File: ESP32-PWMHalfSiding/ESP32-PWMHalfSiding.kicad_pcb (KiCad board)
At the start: 2 copper layers, 115.6 x 130.8 mm, 60 parts, among them IC1 MCT6H, IC2 MCT6H, J1 RJ45, J2 RJ45, P601 C A0 A1 A2 A3 A4 A5 A6 A7, P602 C B0 B1 B2 B3 B4 B5 B6 B7, T1 + 15 in -, T2 + 15 out -, T3 In Track1 Out, T4 Motor 1, T5 Motor 2, T6 In Track1 Out, T601 + 12V -, U0 ESP32_DEVKIT_C or TTGO-T1, U0A TTGO-T1, U1 TCAN332DR, U2 SN65HVD233-HT, U3 LM2574N-5.0, U601 PCA9685, U602 TBD62X83A, U603 TBD62X83A, U7 TC4428, U8 TC4428, U9 74HCT00

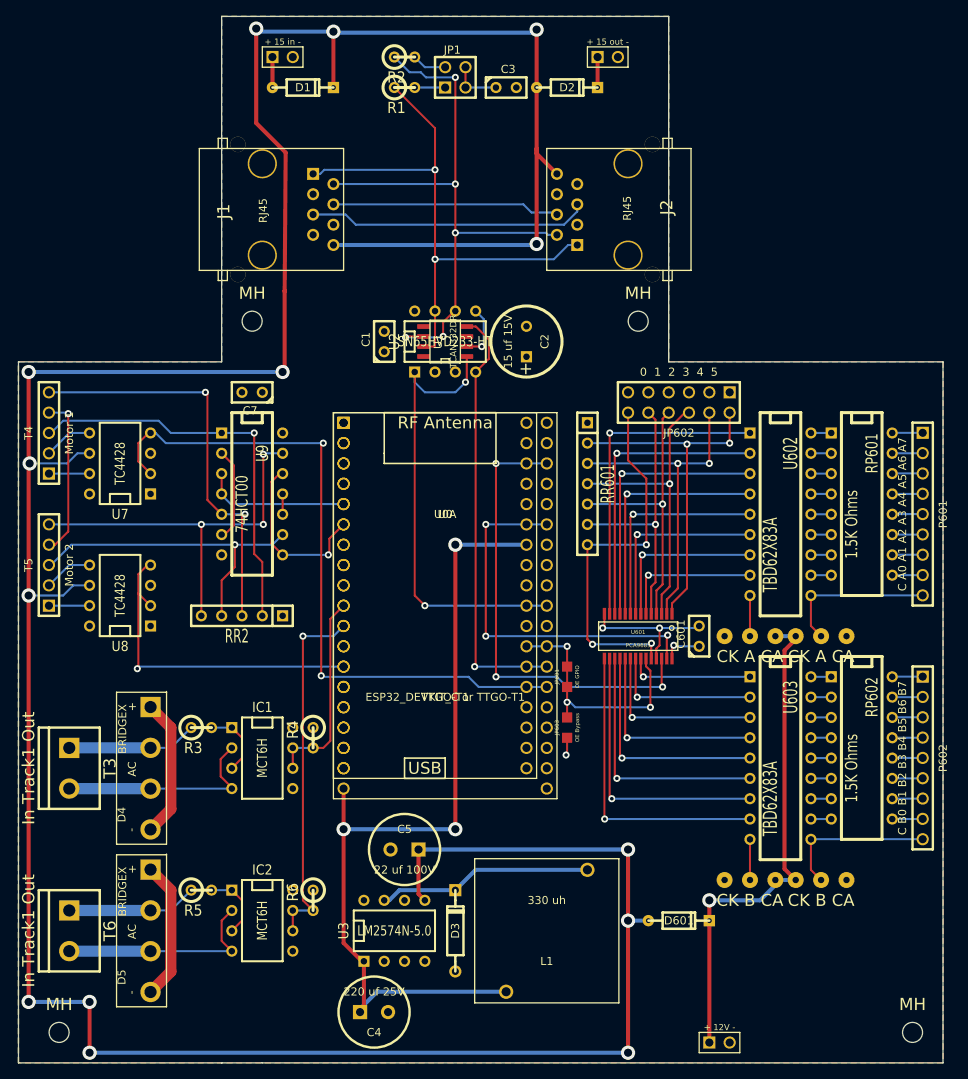
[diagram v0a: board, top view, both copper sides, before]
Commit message: Remove unneeded address jumpers from ESP32-PWMHalfSiding and fixup board part labels.
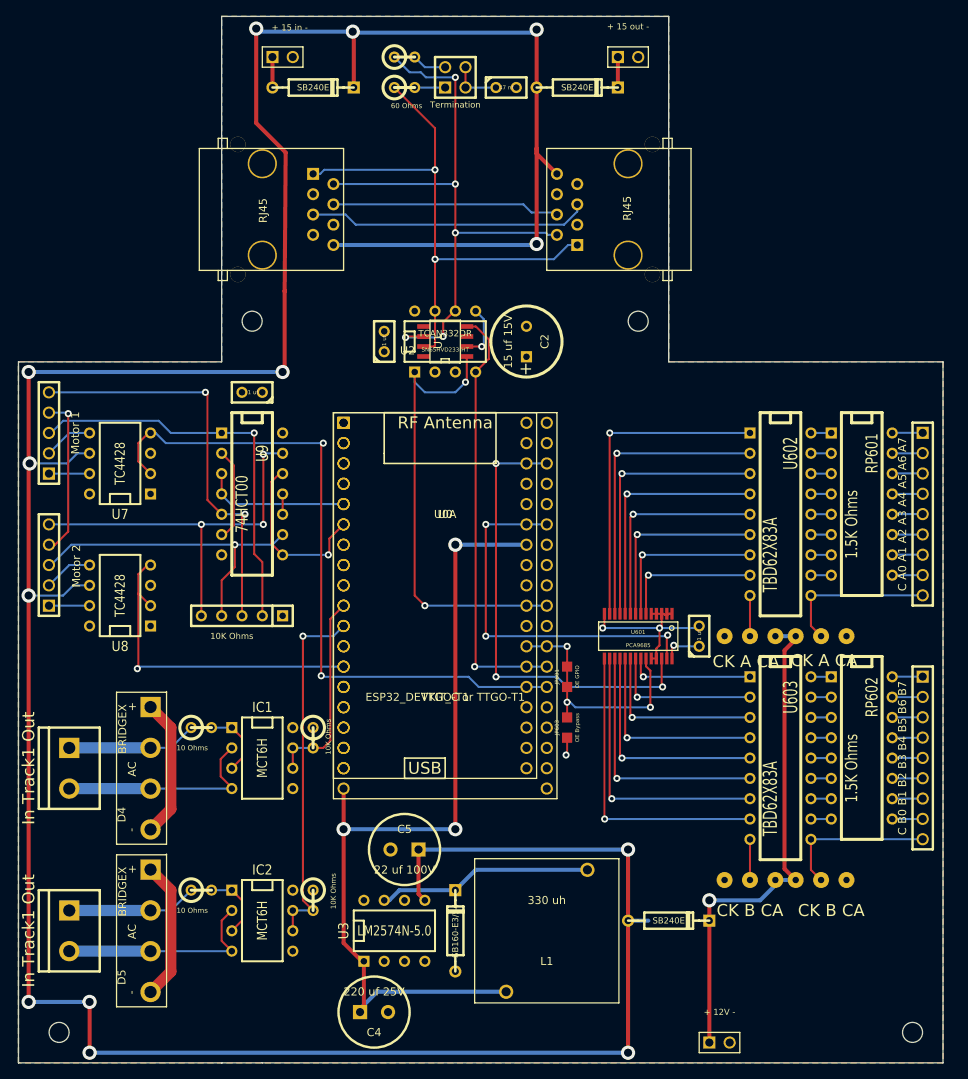
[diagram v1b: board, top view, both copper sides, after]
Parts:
- removed JP602: 0 1 2 3 4 5, pin_array_6x2
- removed RR601: 10K Ohms, SIL-7
- D1, D2, D601: footprint DO-35 -> DO-41
- moved T2 2.54 mm to (160.0, 21.6)
- moved D1 1.27 mm to (120.7, 25.4)
- moved D601 1.27 mm to (165.1, 129.5)
- moved D2 1.27 mm to (153.7, 25.4)
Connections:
- U601 pad 1: N-00000125 -> GND
- U601 pad 2: N-00000110 (its old number) -> GND
- U601 pad 24: N-00000124 -> GND
- U601 pad 3: N-00000111 (its old number) -> GND
- U601 pad 4: N-00000112 (its old number) -> GND
- U601 pad 5: N-00000113 (its old number) -> GND
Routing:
- net N-00000124: track 46.9 -> 0.00 mm, vias 3 -> 0
- net N-00000125: track 43.7 -> 0.00 mm, vias 2 -> 0
- net N-00000110 (its old number): track 41.0 -> 0.00 mm, vias 2 -> 0
- net N-00000111 (its old number): track 37.1 -> 0.00 mm, vias 1 -> 0
- net N-00000112 (its old number): track 35.2 -> 0.00 mm, vias 1 -> 0
- net N-00000113 (its old number): track 34.2 -> 0.00 mm, vias 1 -> 0
- net GND: track 47.9 -> 53.7 mm
- net CAN +12V: vias 14 -> 13

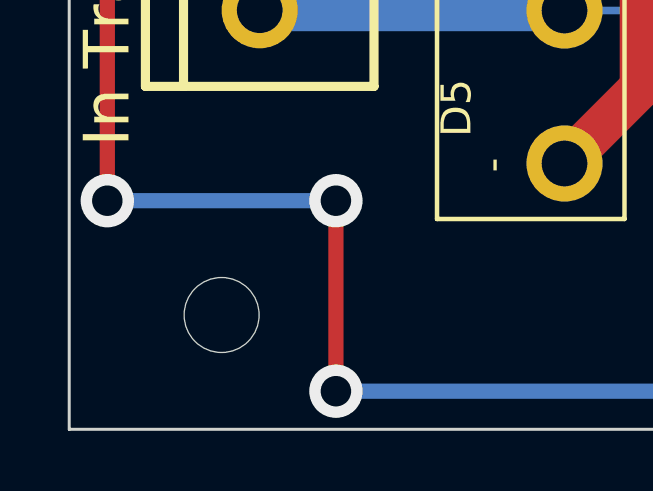
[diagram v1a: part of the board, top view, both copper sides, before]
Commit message: Add dimensions and move one mounting hole on ESP32-PWMHalfSiding.
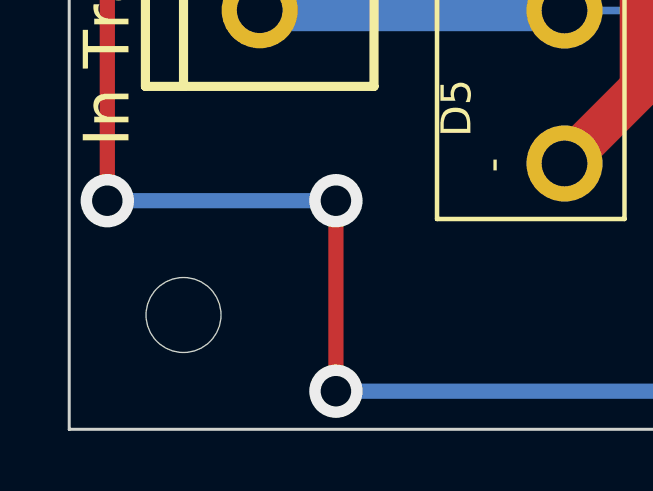
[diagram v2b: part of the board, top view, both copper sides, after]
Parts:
- moved MH 1.27 mm to (87.6, 143.5)
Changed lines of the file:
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@@
     (links 214)
     (no_connects 0)
-    (area 57.265994 16.256 227.412126 148.27758)
+    (area 55.995994 12.390001 227.412126 161.45)
     (thickness 1.6)
-    (drawings 21)
+    (drawings 35)
     (tracks 507)
     (zones 0)
@@
   )
   (module MountingHole_2-5mm_RevA_Date21Jun2010 (layer F.Cu)
-    (at 88.9 143.51)
+    (at 87.63 143.51)
     (descr "Mounting hole, Befestigungsbohrung, 2,5mm, No Annular, Kein Restring,")
     (tags "Mounting hole, Befestigungsbohrung, 2,5mm, No Annular, Kein Restring,")
@@
     )
   )
+  (dimension 3.81 (width 0.3) (layer Cmts.User)
+    (gr_text "3.810 mm" (at 79.930001 145.415 270) (layer Cmts.User)
+      (effects (font (size 1.5 1.5) (thickness 0.3)))
+    )
+    (feature1 (pts (xy 87.63 147.32) (xy 78.580001 147.32)))
+    (feature2 (pts (xy 87.63 143.51) (xy 78.580001 143.51)))
+    (crossbar (pts (xy 81.280001 143.51) (xy 81.280001 147.32)))
+    (arrow1a (pts (xy 81.280001 147.32) (xy 80.693581 146.193497)))
+    (arrow1b (pts (xy 81.280001 147.32) (xy 81.866421 146.193497)))
+    (arrow2a (pts (xy 81.280001 143.51) (xy 80.693581 144.636503)))
+    (arrow2b (pts (xy 81.280001 143.51) (xy 81.866421 144.636503)))
+  )
+  (dimension 3.81 (width 0.3) (layer Cmts.User)
+    (gr_text "3.810 mm" (at 204.549999 145.415 270) (layer Cmts.User)
+      (effects (font (size 1.5 1.5) (thickness 0.3)))
+    )
+    (feature1 (pts (xy 195.58 147.32) (xy 205.899999 147.32)))
+    (feature2 (pts (xy 195.58 143.51) (xy 205.899999 143.51)))
+    (crossbar (pts (xy 203.199999 143.51) (xy 203.199999 147.32)))
+    (arrow1a (pts (xy 203.199999 147.32) (xy 202.613579 146.193497)))
+    (arrow1b (pts (xy 203.199999 147.32) (xy 203.786419 146.193497)))
+    (arrow2a (pts (xy 203.199999 143.51) (xy 202.613579 144.636503)))
+    (arrow2b (pts (xy 203.199999 143.51) (xy 203.786419 144.636503)))
+  )
+  (dimension 107.95 (width 0.3) (layer Cmts.User)
+    (gr_text "107.950 mm" (at 141.605 152.479999) (layer Cmts.User)
+      (effects (font (size 1.5 1.5) (thickness 0.3)))
+    )
+    (feature1 (pts (xy 195.58 143.51) (xy 195.58 153.829999)))
+    (feature2 (pts (xy 87.63 143.51) (xy 87.63 153.829999)))
+    (crossbar (pts (xy 87.63 151.129999) (xy 195.58 151.129999)))
+    (arrow1a (pts (xy 195.58 151.129999) (xy 194.453497 151.716419)))
+    (arrow1b (pts (xy 195.58 151.129999) (xy 194.453497 150.543579)))
+    (arrow2a (pts (xy 87.63 151.129999) (xy 88.756503 151.716419)))
+    (arrow2b (pts (xy 87.63 151.129999) (xy 88.756503 150.543579)))
+  )
+  (dimension 3.81 (width 0.3) (layer Cmts.User)
+    (gr_text "3.810 mm" (at 85.725 152.479999) (layer Cmts.User)
+      (effects (font (size 1.5 1.5) (thickness 0.3)))
+    )
+    (feature1 (pts (xy 83.82 143.51) (xy 83.82 153.829999)))
+    (feature2 (pts (xy 87.63 143.51) (xy 87.63 153.829999)))
+    (crossbar (pts (xy 87.63 151.129999) (xy 83.82 151.129999)))
+    (arrow1a (pts (xy 83.82 151.129999) (xy 84.946503 150.543579)))
+    (arrow1b (pts (xy 83.82 151.129999) (xy 84.946503 151.716419)))
+    (arrow2a (pts (xy 87.63 151.129999) (xy 86.503497 150.543579)))
+    (arrow2b (pts (xy 87.63 151.129999) (xy 86.503497 151.716419)))
+  )
+  (dimension 3.81 (width 0.3) (layer Cmts.User)
+    (gr_text "3.810 mm" (at 197.485 152.479999) (layer Cmts.User)
+      (effects (font (size 1.5 1.5) (thickness 0.3)))
+    )
+    (feature1 (pts (xy 199.39 143.51) (xy 199.39 153.829999)))
+    (feature2 (pts (xy 195.58 143.51) (xy 195.58 153.829999)))
+    (crossbar (pts (xy 195.58 151.129999) (xy 199.39 151.129999)))
+    (arrow1a (pts (xy 199.39 151.129999) (xy 198.263497 151.716419)))
+    (arrow1b (pts (xy 199.39 151.129999) (xy 198.263497 150.543579)))
+    (arrow2a (pts (xy 195.58 151.129999) (xy 196.706503 151.716419)))
+    (arrow2b (pts (xy 195.58 151.129999) (xy 196.706503 150.543579)))
+  )
+  (dimension 3.81 (width 0.3) (layer Cmts.User)
+    (gr_text "3.810 mm" (at 111.125 13.890001) (layer Cmts.User)
+      (effects (font (size 1.5 1.5) (thickness 0.3)))
+    )
+    (feature1 (pts (xy 109.22 54.61) (xy 109.22 12.540001)))
+    (feature2 (pts (xy 113.03 54.61) (xy 113.03 12.540001)))
+    (crossbar (pts (xy 113.03 15.240001) (xy 109.22 15.240001)))
+    (arrow1a (pts (xy 109.22 15.240001) (xy 110.346503 14.653581)))
+    (arrow1b (pts (xy 109.22 15.240001) (xy 110.346503 15.826421)))
+    (arrow2a (pts (xy 113.03 15.240001) (xy 111.903497 14.653581)))
+    (arrow2b (pts (xy 113.03 15.240001) (xy 111.903497 15.826421)))
+  )
+  (dimension 25.4 (width 0.3) (layer Cmts.User)
+    (gr_text "25.400 mm" (at 96.520001 13.890001) (layer Cmts.User)
+      (effects (font (size 1.5 1.5) (thickness 0.3)))
+    )
+    (feature1 (pts (xy 109.22 59.69) (xy 109.220001 12.540001)))
+    (feature2 (pts (xy 83.82 59.69) (xy 83.820001 12.540001)))
+    (crossbar (pts (xy 83.820001 15.240001) (xy 109.220001 15.240001)))
+    (arrow1a (pts (xy 109.220001 15.240001) (xy 108.093498 15.826421)))
+    (arrow1b (pts (xy 109.220001 15.240001) (xy 108.093498 14.653581)))
+    (arrow2a (pts (xy 83.820001 15.240001) (xy 84.946504 15.826421)))
+    (arrow2b (pts (xy 83.820001 15.240001) (xy 84.946504 14.653581)))
+  )
+  (dimension 34.29 (width 0.3) (layer Cmts.User)
+    (gr_text "34.290 mm" (at 182.245001 13.890001) (layer Cmts.User)
+      (effects (font (size 1.5 1.5) (thickness 0.3)))
+    )
+    (feature1 (pts (xy 199.39 59.69) (xy 199.390001 12.540001)))
+    (feature2 (pts (xy 165.1 59.69) (xy 165.100001 12.540001)))
+    (crossbar (pts (xy 165.100001 15.240001) (xy 199.390001 15.240001)))
+    (arrow1a (pts (xy 199.390001 15.240001) (xy 198.263498 15.826421)))
+    (arrow1b (pts (xy 199.390001 15.240001) (xy 198.263498 14.653581)))
+    (arrow2a (pts (xy 165.100001 15.240001) (xy 166.226504 15.826421)))
+    (arrow2b (pts (xy 165.100001 15.240001) (xy 166.226504 14.653581)))
+  )
+  (dimension 3.81 (width 0.3) (layer Cmts.User)
+    (gr_text "3.810 mm" (at 163.195001 13.890001) (layer Cmts.User)
+      (effects (font (size 1.5 1.5) (thickness 0.3)))
+    )
+    (feature1 (pts (xy 165.1 54.61) (xy 165.100001 12.540001)))
+    (feature2 (pts (xy 161.29 54.61) (xy 161.290001 12.540001)))
+    (crossbar (pts (xy 161.290001 15.240001) (xy 165.100001 15.240001)))
+    (arrow1a (pts (xy 165.100001 15.240001) (xy 163.973498 15.826421)))
+    (arrow1b (pts (xy 165.100001 15.240001) (xy 163.973498 14.653581)))
+    (arrow2a (pts (xy 161.290001 15.240001) (xy 162.416504 15.826421)))
+    (arrow2b (pts (xy 161.290001 15.240001) (xy 162.416504 14.653581)))
+  )
+  (dimension 38.1 (width 0.3) (layer Cmts.User)
+    (gr_text "38.100 mm" (at 174.07 35.56 90) (layer Cmts.User)
+      (effects (font (size 1.5 1.5) (thickness 0.3)))
+    )
+    (feature1 (pts (xy 161.29 16.51) (xy 175.42 16.51)))
+    (feature2 (pts (xy 161.29 54.61) (xy 175.42 54.61)))
+    (crossbar (pts (xy 172.72 54.61) (xy 172.72 16.51)))
+    (arrow1a (pts (xy 172.72 16.51) (xy 173.30642 17.636503)))
+    (arrow1b (pts (xy 172.72 16.51) (xy 172.13358 17.636503)))
+    (arrow2a (pts (xy 172.72 54.61) (xy 173.30642 53.483497)))
+    (arrow2b (pts (xy 172.72 54.61) (xy 172.13358 53.483497)))
+  )
+  (dimension 88.9 (width 0.3) (layer Cmts.User)
+    (gr_text "88.900 mm" (at 204.549999 99.060003 270) (layer Cmts.User)
+      (effects (font (size 1.5 1.5) (thickness 0.3)))
+    )
+    (feature1 (pts (xy 161.29 143.51) (xy 205.899999 143.510003)))
+    (feature2 (pts (xy 161.29 54.61) (xy 205.899999 54.610003)))
+    (crossbar (pts (xy 203.199999 54.610003) (xy 203.199999 143.510003)))
+    (arrow1a (pts (xy 203.199999 143.510003) (xy 202.613579 142.3835)))
+    (arrow1b (pts (xy 203.199999 143.510003) (xy 203.786419 142.3835)))
+    (arrow2a (pts (xy 203.199999 54.610003) (xy 202.613579 55.736506)))
+    (arrow2b (pts (xy 203.199999 54.610003) (xy 203.786419 55.736506)))
+  )
+  (dimension 48.26 (width 0.3) (layer Cmts.User)
+    (gr_text "48.260 mm" (at 137.160001 13.890001) (layer Cmts.User)
+      (effects (font (size 1.5 1.5) (thickness 0.3)))
+    )
+    (feature1 (pts (xy 161.29 54.61) (xy 161.290001 12.540001)))
+    (feature2 (pts (xy 113.03 54.61) (xy 113.030001 12.540001)))
+    (crossbar (pts (xy 113.030001 15.240001) (xy 161.290001 15.240001)))
+    (arrow1a (pts (xy 161.290001 15.240001) (xy 160.163498 15.826421)))
+    (arrow1b (pts (xy 161.290001 15.240001) (xy 160.163498 14.653581)))
+    (arrow2a (pts (xy 113.030001 15.240001) (xy 114.156504 15.826421)))
+    (arrow2b (pts (xy 113.030001 15.240001) (xy 114.156504 14.653581)))
+  )
+  (dimension 130.81 (width 0.3) (layer Cmts.User)
+    (gr_text "130.810 mm" (at 210.899999 81.915003 270) (layer Cmts.User)
+      (effects (font (size 1.5 1.5) (thickness 0.3)))
+    )
+    (feature1 (pts (xy 165.1 147.32) (xy 212.249999 147.320003)))
+    (feature2 (pts (xy 165.1 16.51) (xy 212.249999 16.510003)))
+    (crossbar (pts (xy 209.549999 16.510003) (xy 209.549999 147.320003)))
+    (arrow1a (pts (xy 209.549999 147.320003) (xy 208.963579 146.1935)))
+    (arrow1b (pts (xy 209.549999 147.320003) (xy 210.136419 146.1935)))
+    (arrow2a (pts (xy 209.549999 16.510003) (xy 208.963579 17.636506)))
+    (arrow2b (pts (xy 209.549999 16.510003) (xy 210.136419 17.636506)))
+  )
+  (dimension 115.57 (width 0.3) (layer Cmts.User)
+    (gr_text "115.570 mm" (at 141.604996 160.099999) (layer Cmts.User)
+      (effects (font (size 1.5 1.5) (thickness 0.3)))
+    )
+    (feature1 (pts (xy 199.39 59.69) (xy 199.389996 161.449999)))
+    (feature2 (pts (xy 83.82 59.69) (xy 83.819996 161.449999)))
+    (crossbar (pts (xy 83.819996 158.749999) (xy 199.389996 158.749999)))
+    (arrow1a (pts (xy 199.389996 158.749999) (xy 198.263493 159.336419)))
+    (arrow1b (pts (xy 199.389996 158.749999) (xy 198.263493 158.163579)))
+    (arrow2a (pts (xy 83.819996 158.749999) (xy 84.946499 159.336419)))
+    (arrow2b (pts (xy 83.819996 158.749999) (xy 84.946499 158.163579)))
+  )
   (gr_text USB (at 134.62 110.49) (layer F.SilkS)
